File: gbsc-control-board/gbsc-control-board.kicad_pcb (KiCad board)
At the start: 2 copper layers, 17 parts, among them J1 Solder_Pad_2x4mm, J2 Solder_Pad_2x4mm, J3 Solder_Pad_2x4mm, J4 Screw_Terminal_01x03, J5 JST B4B-XH-A, J6 JST B2B-XH-A, J7 JST B2B-XH-A, J8 JST B2B-XH-A, SW1 EC11 Rotary Encoder, U1 WeMos_D1_mini, U2 SSD1306_OLED

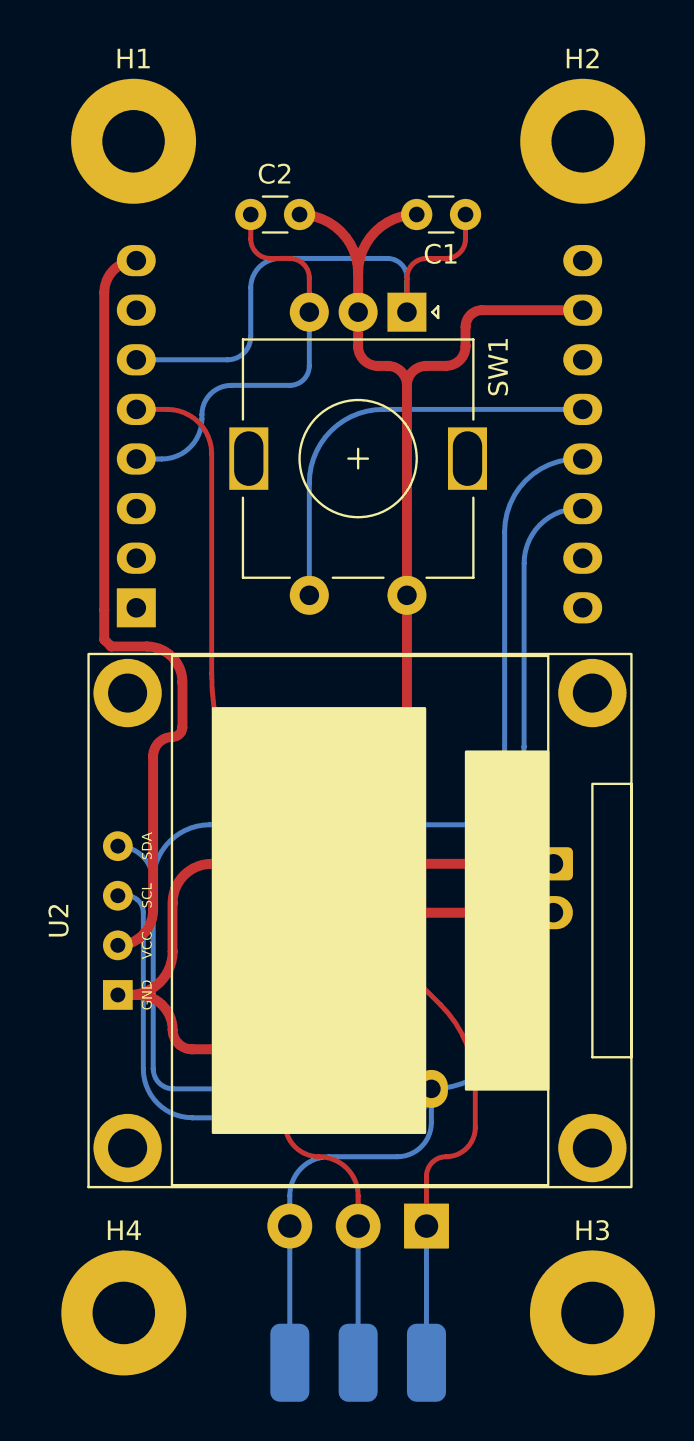
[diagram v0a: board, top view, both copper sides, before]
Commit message: Vertical mounted layout nearly done
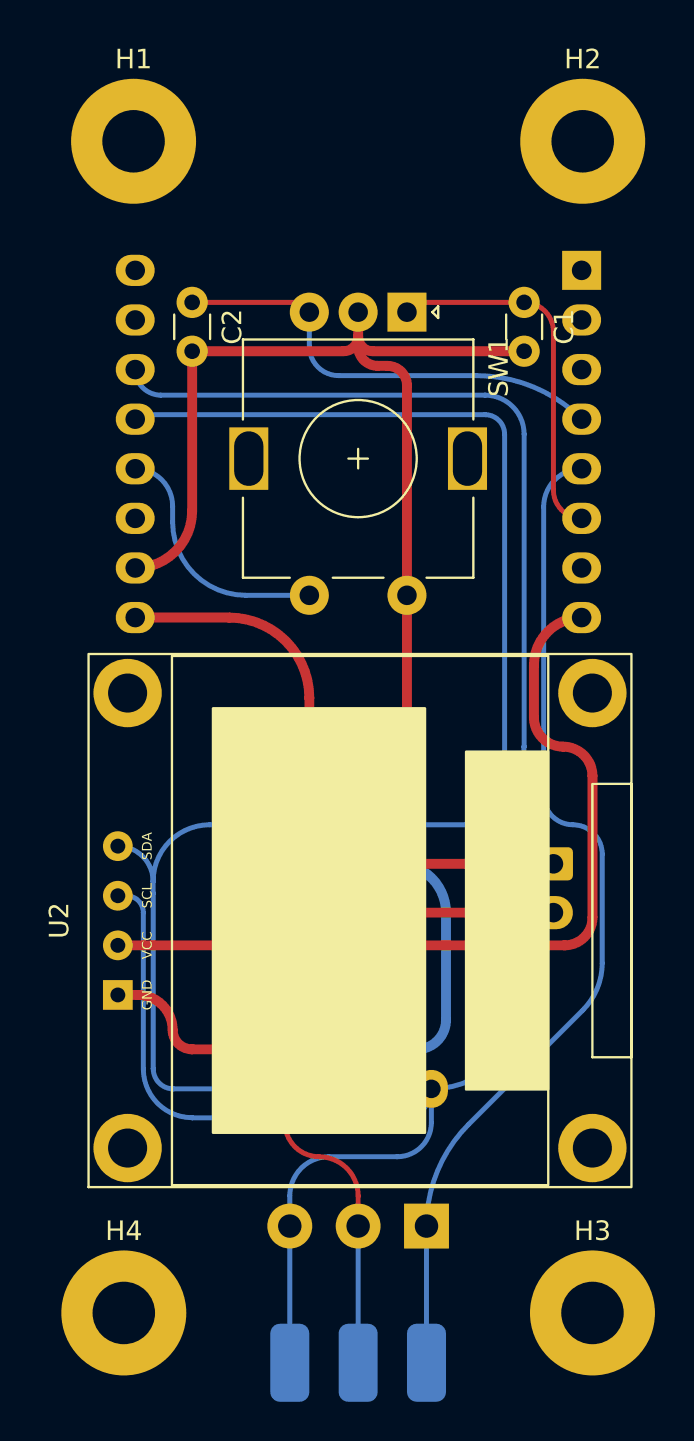
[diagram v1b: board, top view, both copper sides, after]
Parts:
- moved U1 28.6 mm to (88.4, 72.6), turned to 180 degrees
- moved C1 5.41 mm to (85.5, 74.2), turned to -90 degrees
- moved C2 5.41 mm to (68.5, 74.2), turned to -90 degrees
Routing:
- net +5V: track 16.0 -> 40.0 mm
- net /SCL: track 80.1 -> 103.9 mm
- net /SDA: track 75.3 -> 93.8 mm
- net GND: track 96.3 -> 108.2 mm
- net /Rotary_Switch: track 21.8 -> 12.7 mm
- net /Rotary_A: track 27.1 -> 19.1 mm
- net /DebugPin: track 57.6 -> 51.9 mm
- net +3V3: track 40.6 -> 43.3 mm
- net /Rotary_B: track 21.3 -> 23.3 mm
